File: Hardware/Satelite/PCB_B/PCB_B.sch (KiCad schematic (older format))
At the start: 34 parts, among them IC1 MCP1642B-50I_MS, J1 Conector_PCB_B-C, J2 Conector_PCB_A-B, M1 Spacer, M2 Spacer, M3 Spacer, Q1 SSM3J338R,LF, U1 MIC5323-3.3YD5_TR

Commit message: Arreglo de mosfet en PCB_B
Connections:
- wire segments 164 -> 165
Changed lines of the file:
@@
 Text Label 5950 1650 2    50   ~ 0
 BATT_INTERNO
-$Comp
-L Device:D_Schottky D1
-U 1 1 5CD2E872
-P 6800 1450
-F 0 "D1" V 6846 1371 50  0000 R CNN
-F 1 "MBRS2040LT3G" V 6755 1371 50  0000 R CNN
-F 2 "Diode_SMD:D_SMB" H 6800 1450 50  0001 C CNN
-F 3 "~" H 6800 1450 50  0001 C CNN
-F 4 "MBRS2040LT3G" V 6800 1450 50  0001 C CNN "Manufacturer Part Number"
-	1    6800 1450
-	0    -1   -1   0
-$EndComp
-Wire Wire Line
-	6400 1250 6400 1300
-Wire Wire Line
-	6800 900  6800 1000
-Wire Wire Line
-	6400 950  6400 900
-Connection ~ 6400 1300
-Wire Wire Line
-	6400 1350 6400 1300
-Wire Wire Line
-	6800 1300 6400 1300
-$Comp
-L power:GND #PWR?
-U 1 1 5CCDA8EC
-P 6800 1000
-AR Path="/5BB6C3A1/5CCDA8EC" Ref="#PWR?"  Part="1"
-AR Path="/5BB6C83B/5CCDA8EC" Ref="#PWR?"  Part="1"
-AR Path="/5BC14C3C/5CCDA8EC" Ref="#PWR?"  Part="1"
-AR Path="/5CCDA8EC" Ref="#PWR017"  Part="1"
-F 0 "#PWR017" H 6800 750 50  0001 C CNN
-F 1 "GND" H 6805 827 50  0000 C CNN
-F 2 "" H 6800 1000 50  0001 C CNN
-F 3 "" H 6800 1000 50  0001 C CNN
-	1    6800 1000
-	1    0    0    -1
-$EndComp
-$Comp
-L Device:R R?
-U 1 1 5CCCB39F
-P 6400 1100
-AR Path="/5BA17F9C/5CCCB39F" Ref="R?"  Part="1"
-AR Path="/5BA1A7F9/5CCCB39F" Ref="R?"  Part="1"
-AR Path="/5BA1A77A/5CCCB39F" Ref="R?"  Part="1"
-AR Path="/5CCCB39F" Ref="R11"  Part="1"
-AR Path="/5BB1631B/5CCCB39F" Ref="R?"  Part="1"
-AR Path="/5BC28DAC/5CCCB39F" Ref="R?"  Part="1"
-F 0 "R11" V 6500 1100 50  0000 L CNN
-F 1 "10k" V 6300 1100 50  0000 L CNN
-F 2 "Capacitor_SMD:C_0603_1608Metric_Pad1.05x0.95mm_HandSolder" V 6330 1100 50  0001 C CNN
-F 3 "~" H 6400 1100 50  0001 C CNN
-F 4 "RC0603JR-0710KL" V 6400 1100 50  0001 C CNN "Manufacturer Part Number"
-	1    6400 1100
-	1    0    0    -1
-$EndComp
 Wire Wire Line
 	5950 1650 5250 1650
-$Comp
-L SamacSys_Parts:SSM3J338R,LF Q1
-U 1 1 5CCA0FA0
-P 6400 1350
-F 0 "Q1" V 6875 1450 50  0000 C CNN
-F 1 "SSM3J338R,LF" V 6966 1450 50  0000 C CNN
-F 2 "SamacSys_Parts:SSM3J332RLFT" H 6850 1300 50  0001 L CNN
-F 3 "http://toshiba.semicon-storage.com/info/docget.jsp?did=30384&prodName=SSM3J338R" H 6850 1200 50  0001 L CNN
-F 4 "MOSFET Small-signal MOSFET Vdss= -12V, ID= -6A" H 6850 1100 50  0001 L CNN "Description"
-F 5 "Toshiba" H 6850 900 50  0001 L CNN "Manufacturer_Name"
-F 6 "SSM3J338R,LF" H 6850 800 50  0001 L CNN "Manufacturer Part Number"
-F 7 "SSM3J338R,LF" H 6850 500 50  0001 L CNN "Arrow Part Number"
-F 8 "https://www.arrow.com/en/products/ssm3j338rlf/toshiba" H 6850 400 50  0001 L CNN "Arrow Price/Stock"
-	1    6400 1350
-	0    1    1    0
-$EndComp
 $Sheet
 S 3350 1450 650  650
@@
 Wire Wire Line
 	4000 1650 4400 1650
-Wire Wire Line
-	6400 1300 6100 1300
 $Comp
 L power:VBUS #PWR0111
@@
 	1    0    0    -1
 $EndComp
-Wire Wire Line
-	6400 900  6800 900
 Wire Wire Line
 	3150 1000 3150 1550
@@
 Wire Wire Line
 	4400 1650 4500 1650
-$Comp
-L power:VBUS #PWR08
-U 1 1 5CE2ECED
-P 6100 1050
-F 0 "#PWR08" H 6100 900 50  0001 C CNN
-F 1 "VBUS" H 6114 1225 50  0000 C CNN
-F 2 "" H 6100 1050 50  0001 C CNN
-F 3 "" H 6100 1050 50  0001 C CNN
-	1    6100 1050
-	1    0    0    -1
-$EndComp
-Wire Wire Line
-	6100 1300 6100 1050
 Wire Wire Line
 	5950 2100 5250 2100
@@
 Wire Wire Line
 	6800 1600 6800 1650
+Wire Wire Line
+	6100 1300 6100 1050
+$Comp
+L power:VBUS #PWR08
+U 1 1 5CE2ECED
+P 6100 1050
+F 0 "#PWR08" H 6100 900 50  0001 C CNN
+F 1 "VBUS" H 6114 1225 50  0000 C CNN
+F 2 "" H 6100 1050 50  0001 C CNN
+F 3 "" H 6100 1050 50  0001 C CNN
+	1    6100 1050
+	1    0    0    -1
+$EndComp
+Wire Wire Line
+	6400 900  6800 900
+Wire Wire Line
+	6400 1300 6100 1300
+$Comp
+L Device:R R?
+U 1 1 5CCCB39F
+P 6400 1100
+AR Path="/5BA17F9C/5CCCB39F" Ref="R?"  Part="1"
+AR Path="/5BA1A7F9/5CCCB39F" Ref="R?"  Part="1"
+AR Path="/5BA1A77A/5CCCB39F" Ref="R?"  Part="1"
+AR Path="/5CCCB39F" Ref="R11"  Part="1"
+AR Path="/5BB1631B/5CCCB39F" Ref="R?"  Part="1"
+AR Path="/5BC28DAC/5CCCB39F" Ref="R?"  Part="1"
+F 0 "R11" V 6500 1100 50  0000 L CNN
+F 1 "10k" V 6300 1100 50  0000 L CNN
+F 2 "Capacitor_SMD:C_0603_1608Metric_Pad1.05x0.95mm_HandSolder" V 6330 1100 50  0001 C CNN
+F 3 "~" H 6400 1100 50  0001 C CNN
+F 4 "RC0603JR-0710KL" V 6400 1100 50  0001 C CNN "Manufacturer Part Number"
+	1    6400 1100
+	1    0    0    -1
+$EndComp
+$Comp
+L power:GND #PWR?
+U 1 1 5CCDA8EC
+P 6800 1000
+AR Path="/5BB6C3A1/5CCDA8EC" Ref="#PWR?"  Part="1"
+AR Path="/5BB6C83B/5CCDA8EC" Ref="#PWR?"  Part="1"
+AR Path="/5BC14C3C/5CCDA8EC" Ref="#PWR?"  Part="1"
+AR Path="/5CCDA8EC" Ref="#PWR017"  Part="1"
+F 0 "#PWR017" H 6800 750 50  0001 C CNN
+F 1 "GND" H 6805 827 50  0000 C CNN
+F 2 "" H 6800 1000 50  0001 C CNN
+F 3 "" H 6800 1000 50  0001 C CNN
+	1    6800 1000
+	1    0    0    -1
+$EndComp
+Wire Wire Line
+	6800 1300 6600 1300
+Connection ~ 6400 1300
+Wire Wire Line
+	6400 950  6400 900
+Wire Wire Line
+	6800 900  6800 1000
+Wire Wire Line
+	6400 1250 6400 1300
+$Comp
+L Device:D_Schottky D1
+U 1 1 5CD2E872
+P 6800 1450
+F 0 "D1" V 6846 1371 50  0000 R CNN
+F 1 "MBRS2040LT3G" V 6755 1371 50  0000 R CNN
+F 2 "Diode_SMD:D_SMB" H 6800 1450 50  0001 C CNN
+F 3 "~" H 6800 1450 50  0001 C CNN
+F 4 "MBRS2040LT3G" V 6800 1450 50  0001 C CNN "Manufacturer Part Number"
+	1    6800 1450
+	0    -1   -1   0
+$EndComp
 Connection ~ 6800 1650
+$Comp
+L SamacSys_Parts:SSM3J338R,LF Q1
+U 1 1 5CCA0FA0
+P 6600 1350
+F 0 "Q1" V 7075 1450 50  0000 C CNN
+F 1 "SSM3J338R,LF" V 7166 1450 50  0000 C CNN
+F 2 "SamacSys_Parts:SSM3J332RLFT" H 7050 1300 50  0001 L CNN
+F 3 "http://toshiba.semicon-storage.com/info/docget.jsp?did=30384&prodName=SSM3J338R" H 7050 1200 50  0001 L CNN
+F 4 "MOSFET Small-signal MOSFET Vdss= -12V, ID= -6A" H 7050 1100 50  0001 L CNN "Description"
+F 5 "Toshiba" H 7050 900 50  0001 L CNN "Manufacturer_Name"
+F 6 "SSM3J338R,LF" H 7050 800 50  0001 L CNN "Manufacturer Part Number"
+F 7 "SSM3J338R,LF" H 7050 500 50  0001 L CNN "Arrow Part Number"
+F 8 "https://www.arrow.com/en/products/ssm3j338rlf/toshiba" H 7050 400 50  0001 L CNN "Arrow Price/Stock"
+	1    6600 1350
+	0    -1   1    0
+$EndComp
+Wire Wire Line
+	6600 1350 6600 1300
+Connection ~ 6600 1300
+Wire Wire Line
+	6600 1300 6400 1300
 $EndSCHEMATC

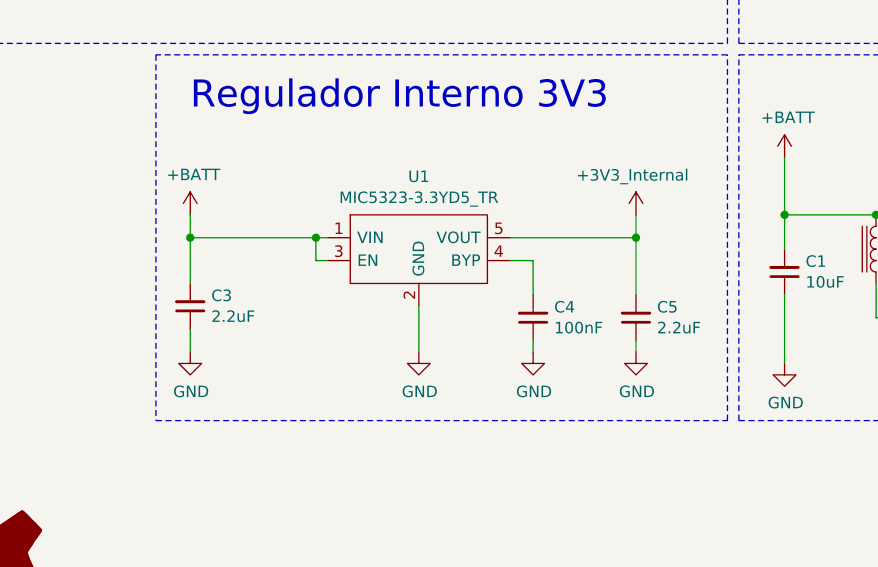
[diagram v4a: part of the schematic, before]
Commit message: Nuevo LDO de más corriente para 3.3V internos en PCB_B
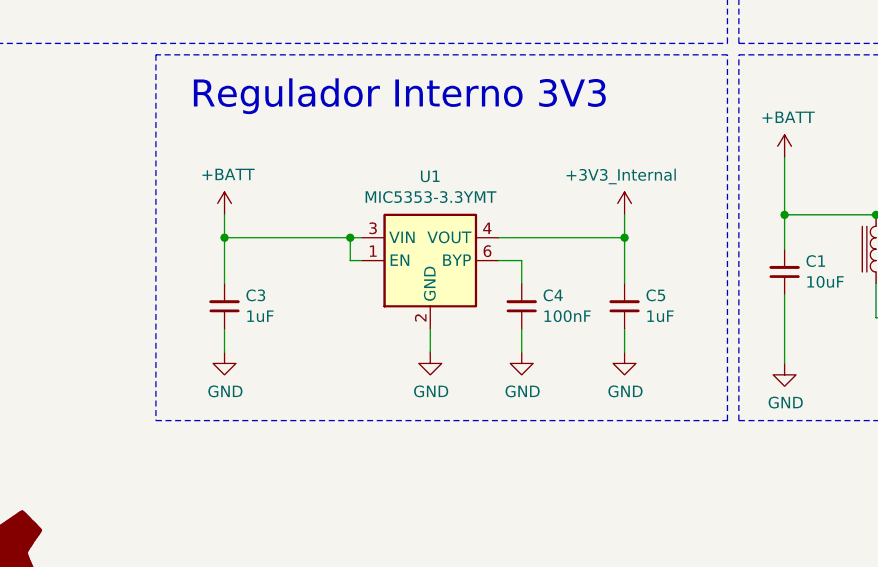
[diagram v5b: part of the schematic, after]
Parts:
- removed U1: MIC5323-3.3YD5_TR, SamacSys_Parts:SOT95P280X100-5N, symbol SamacSys_Parts:MIC5323-3.3YD5_TR
- added U1: MIC5353-3.3YMT, Package_DFN_QFN:MLF-6-1EP_1.6x1.6mm_P0.5mm_EP0.5x1.26mm, symbol Regulator_Linear:MIC5353-3.3YMT
- C3, C5: value 2.2uF -> 1uF; footprint Capacitor_SMD:C_0805_2012Metric_Pad1.15x1.40mm_HandSolder -> Capacitor_SMD:C_0603_1608Metric_Pad1.05x0.95mm_HandSolder; Manufacturer Part Number LMK212B7225KG-T -> LMK107B7105MA-T
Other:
- moved on the sheet: C4

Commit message: Nuevos separadores en PCB_B
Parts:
- M1, M2, M3: Manufacturer Part Number R30-3011202 -> R30-3001202
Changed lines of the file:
@@
 F 2 "AXTEC:Empty_Footprint" H 5200 7150 50  0001 C CNN
 F 3 "https://www.mouser.com/datasheet/2/181/R30-301-1135805.pdf" H 5300 7250 50  0001 C CNN
-F 4 "R30-3011202" H 5379 6855 50  0001 L CNN "Manufacturer Part Number"
+F 4 "R30-3001202" H 5379 6855 50  0001 L CNN "Manufacturer Part Number"
 	1    5300 7000
 	1    0    0    -1
@@
 F 2 "AXTEC:Empty_Footprint" H 5700 7150 50  0001 C CNN
 F 3 "https://www.mouser.com/datasheet/2/181/R30-301-1135805.pdf" H 5800 7250 50  0001 C CNN
-F 4 "R30-3011202" H 5879 6855 50  0001 L CNN "Manufacturer Part Number"
+F 4 "R30-3001202" H 5879 6855 50  0001 L CNN "Manufacturer Part Number"
 	1    5800 7000
 	1    0    0    -1
@@
 F 2 "AXTEC:Empty_Footprint" H 6200 7150 50  0001 C CNN
 F 3 "https://www.mouser.com/datasheet/2/181/R30-301-1135805.pdf" H 6300 7250 50  0001 C CNN
-F 4 "R30-3011202" H 6379 6855 50  0001 L CNN "Manufacturer Part Number"
+F 4 "R30-3001202" H 6379 6855 50  0001 L CNN "Manufacturer Part Number"
 	1    6300 7000
 	1    0    0    -1
